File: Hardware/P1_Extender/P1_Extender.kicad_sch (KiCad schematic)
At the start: 8 parts, among them J1 RJ12, U1 6N137, U2 WeMos_D1_mini, U3 6N137

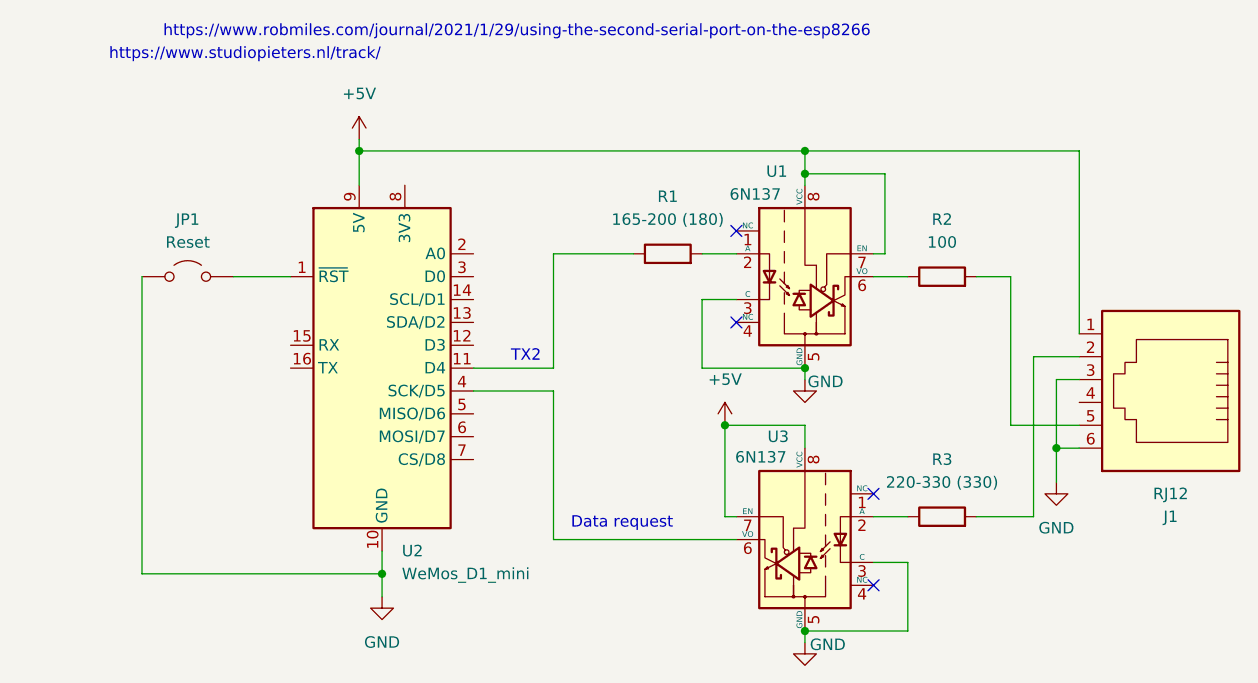
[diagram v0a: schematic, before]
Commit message: Added new hardware version to fix the issues
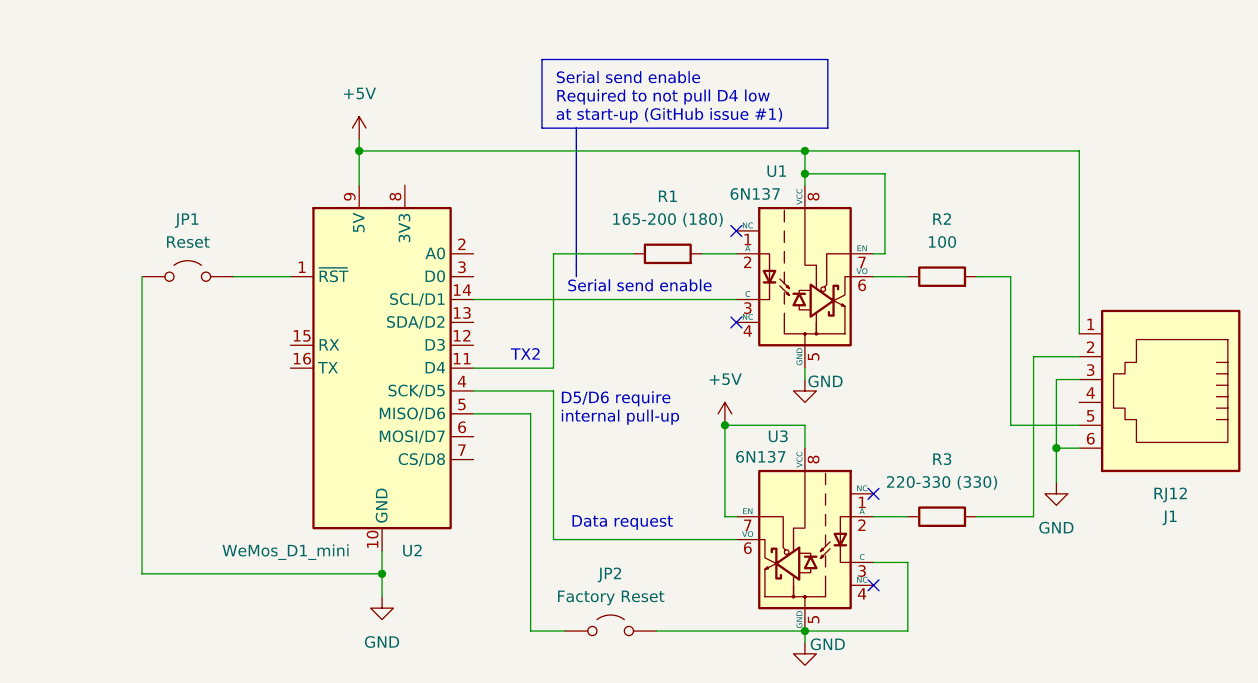
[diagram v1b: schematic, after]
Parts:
- added JP2: Factory Reset, Connector_PinHeader_2.54mm:PinHeader_1x02_P2.54mm_Vertical, symbol Jumper:Jumper_2_Open
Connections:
- net GND: now also JP2.2 (B); no longer U1.3 (C)
- net at U2.14 (SCL/D1): now also U1.3 (C)
- net at U2.5 (MISO/D6): now also JP2.1 (A)
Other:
- note added: "D5/D6 require internal pull-up"
- note added: "Serial send enable"
- note added: "Serial send enable Required to not pull D4 low at start-up (GitHub issue #1)"
- note removed: "https://www.robmiles.com/journal/2021/1/29/using-the-second-serial-port-on-the-esp8266"
- note removed: "https://www.studiopieters.nl/track/"
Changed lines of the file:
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@@
 	(title_block
 		(title "Smartmeter P1 Extender")
-		(date "2025-01-10")
-		(rev "1.0")
+		(date "2025-01-26")
+		(rev "1.1")
 		(company "JMNL Innovation")
 		(comment 1 "Maurice Snoeren")
+		(comment 2 "Added factory reset and fixed issue with D5 driving low at startup (GitHub issue #1).")
 	)
 	(junction
@@
 	)
 	(junction
-		(at 130.81 73.66)
-		(diameter 0)
-		(color 0 0 0 0)
-	)
-	(junction
 		(at 158.75 82.55)
 		(diameter 0)
@@
 	(wire
 		(pts
-			(xy 119.38 73.66) (xy 130.81 73.66)
-		)
-		(stroke
-			(width 0)
-			(type default)
-		)
-	)
-	(wire
-		(pts
 			(xy 121.92 80.01) (xy 130.81 80.01)
 		)
@@
 	(wire
 		(pts
+			(xy 100.33 102.87) (xy 104.14 102.87)
+		)
+		(stroke
+			(width 0)
+			(type default)
+		)
+	)
+	(wire
+		(pts
 			(xy 161.29 82.55) (xy 158.75 82.55)
 		)
@@
 	(wire
 		(pts
-			(xy 123.19 66.04) (xy 119.38 66.04)
+			(xy 114.3 102.87) (xy 130.81 102.87)
+		)
+		(stroke
+			(width 0)
+			(type default)
+		)
+	)
+	(wire
+		(pts
+			(xy 93.98 66.04) (xy 123.19 66.04)
 		)
 		(stroke
@@
 		)
 	)
+	(polyline
+		(pts
+			(xy 105.41 46.99) (xy 105.41 62.23)
+		)
+		(stroke
+			(width 0)
+			(type default)
+		)
+	)
 	(wire
 		(pts
@@
 	(wire
 		(pts
+			(xy 93.98 78.74) (xy 100.33 78.74)
+		)
+		(stroke
+			(width 0)
+			(type default)
+		)
+	)
+	(wire
+		(pts
 			(xy 161.29 69.85) (xy 161.29 49.53)
 		)
@@
 	(wire
 		(pts
-			(xy 119.38 66.04) (xy 119.38 73.66)
-		)
-		(stroke
-			(width 0)
-			(type default)
-		)
-	)
-	(wire
-		(pts
 			(xy 102.87 60.96) (xy 111.76 60.96)
 		)
@@
 	(wire
 		(pts
+			(xy 100.33 78.74) (xy 100.33 102.87)
+		)
+		(stroke
+			(width 0)
+			(type default)
+		)
+	)
+	(polyline
+		(pts
+			(xy 105.41 62.23) (xy 105.41 63.5)
+		)
+		(stroke
+			(width 0)
+			(type default)
+		)
+	)
+	(wire
+		(pts
 			(xy 161.29 49.53) (xy 130.81 49.53)
 		)
@@
 			(width 0)
 			(type default)
+		)
+	)
+	(rectangle
+		(start 101.6 39.37)
+		(end 133.35 46.99)
+		(stroke
+			(width 0)
+			(type default)
+		)
+		(fill
+			(type none)
 		)
 	)
@@
 		)
 	)
+	(text "Serial send enable\nRequired to not pull D4 low\nat start-up (GitHub issue #1)"
+		(exclude_from_sim no)
+		(at 103.124 43.688 0)
+		(effects
+			(font
+				(size 1.27 1.27)
+			)
+			(justify left)
+		)
+	)
 	(text "Data request"
 		(exclude_from_sim no)
@@
 		)
 	)
-	(text "https://www.studiopieters.nl/track/"
+	(text "Serial send enable"
 		(exclude_from_sim no)
-		(at 68.58 38.862 0)
+		(at 104.394 64.77 0)
 		(effects
 			(font
 				(size 1.27 1.27)
 			)
-		)
-	)
-	(text "https://www.robmiles.com/journal/2021/1/29/using-the-second-serial-port-on-the-esp8266"
+			(justify left)
+		)
+	)
+	(text "D5/D6 require\ninternal pull-up"
 		(exclude_from_sim no)
-		(at 98.806 36.322 0)
+		(at 103.632 78.232 0)
 		(effects
 			(font
 				(size 1.27 1.27)
 			)
+			(justify left)
 		)
 	)
@@
 		(on_board yes)
 		(dnp no)
-		(fields_autoplaced yes)
 		(property "Reference" "U2"
 			(at 86.0141 93.98 0)
@@
 		)
 		(property "Value" "WeMos_D1_mini"
-			(at 86.0141 96.52 0)
+			(at 66.04 93.98 0)
 			(effects
 				(font
@@
 					(unit 1)
 				)
+			)
+		)
+	)
+	(symbol
+		(lib_id "Jumper:Jumper_2_Open")
+		(at 109.22 102.87 0)
+		(unit 1)
+		(exclude_from_sim yes)
+		(in_bom yes)
+		(on_board yes)
+		(dnp no)
+		(fields_autoplaced yes)
+		(property "Reference" "JP2"
+			(at 109.22 96.52 0)
+			(effects
+				(font
+					(size 1.27 1.27)
+				)
+			)
+		)
+		(property "Value" "Factory Reset"
+			(at 109.22 99.06 0)
+			(effects
+				(font
+					(size 1.27 1.27)
+				)
+			)
+		)
+		(property "Footprint" "Connector_PinHeader_2.54mm:PinHeader_1x02_P2.54mm_Vertical"
+			(at 109.22 102.87 0)
+			(effects
+				(font
+					(size 1.27 1.27)
+				)
+				(hide yes)
+			)
+		)
+		(property "Datasheet" "~"
+			(at 109.22 102.87 0)
+			(effects
+				(font
+					(size 1.27 1.27)
+				)
+				(hide yes)
+			)
+		)
+		(property "Description" "Jumper, 2-pole, open"
+			(at 109.22 102.87 0)
+			(effects
+				(font
+					(size 1.27 1.27)
+				)
+				(hide yes)
+			)
+		)
+		(pin "1"
+		)
+		(pin "2"
+		)
+		(instances
+			(project "P1_Extender"
+				(path "/62ade568-5571-4643-8346-9fdf82f878c8"
+					(reference "JP2")
+					(unit 1)
+				)
